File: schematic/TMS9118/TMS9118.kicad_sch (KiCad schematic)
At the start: 31 parts, among them CON1 PICERINO-EDGE, J1 Conn_Coaxial, J10 Conn_01x03, J2 Conn_01x02, J3 Conn_01x02, J8 Conn_01x08, J9 Conn_01x08, U1 TMS4416, U14 TMS9118NL, U3 TMS4416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

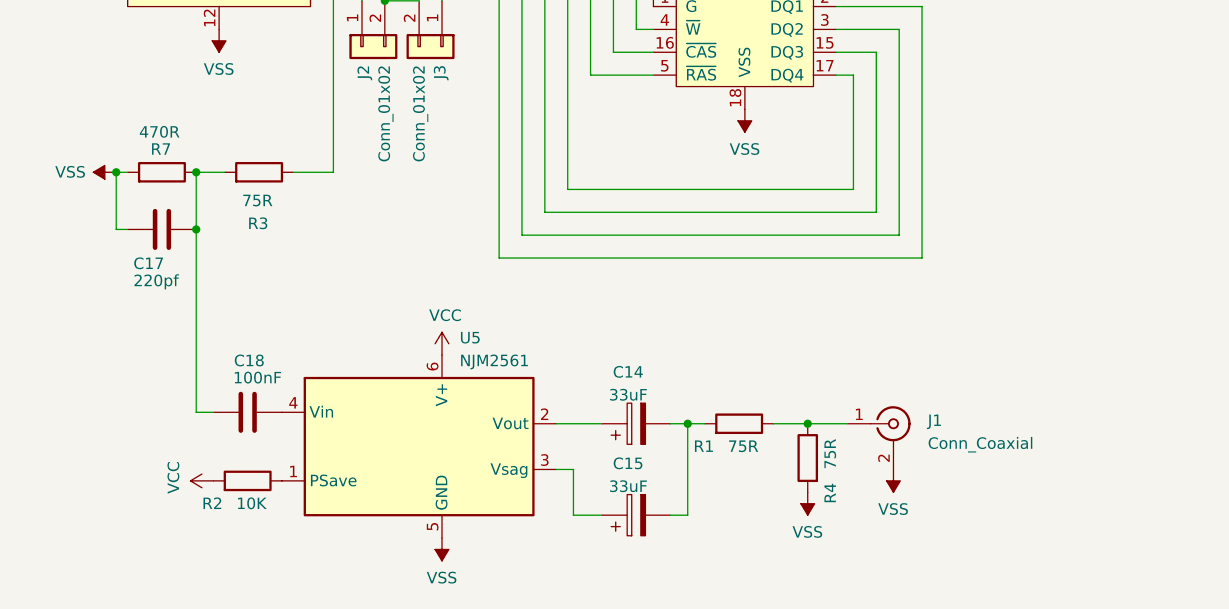
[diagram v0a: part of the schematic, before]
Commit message: added new switch and sample video chip to simplify video output. work in progress.
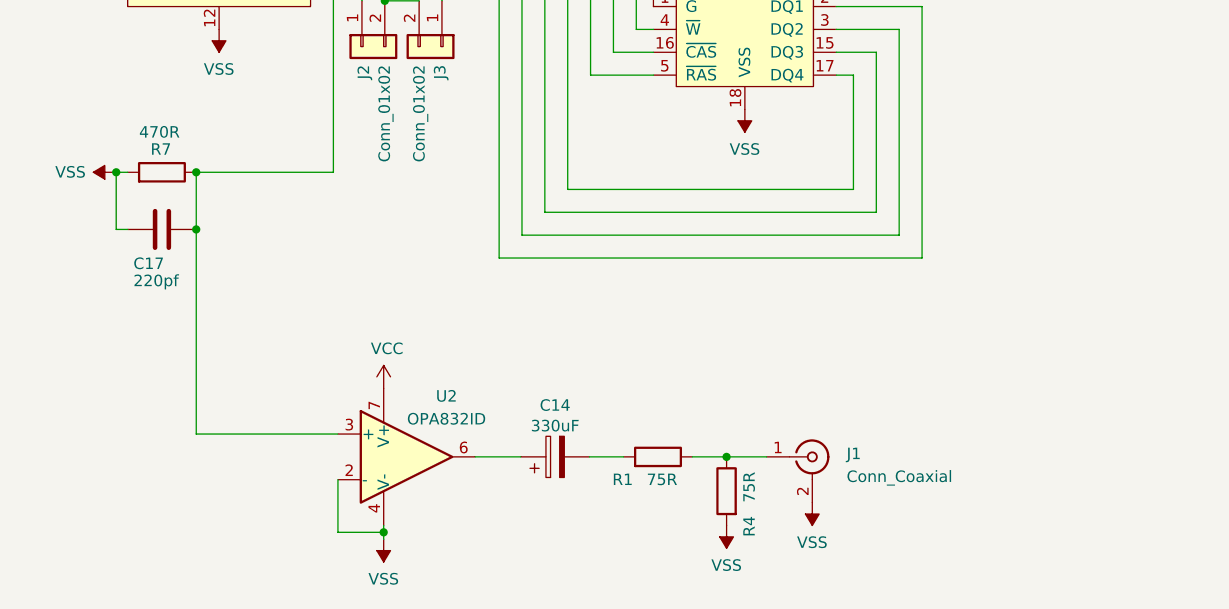
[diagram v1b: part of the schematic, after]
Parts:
- removed C15: 33uF, Capacitor_THT:CP_Radial_D5.0mm_P2.50mm, symbol Device:C_Polarized
- removed C18: 100nF, Capacitor_THT:C_Disc_D4.7mm_W2.5mm_P5.00mm, symbol Device:C
- removed R2: 10K, Resistor_THT:R_Axial_DIN0207_L6.3mm_D2.5mm_P7.62mm_Horizontal, symbol Device:R
- removed R3: 75R, Resistor_THT:R_Axial_DIN0207_L6.3mm_D2.5mm_P7.62mm_Horizontal, symbol Device:R
- removed U5: NJM2561, Package_TO_SOT_SMD:TSOT-23-6, symbol Video_II:NJM2561
- added U2: OPA832ID, Package_SO:SOIC-8_3.9x4.9mm_P1.27mm, symbol Amplifier_Operational:OPA842xD
- C14: value 33uF -> 330uF
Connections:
- net VCC: now also U2.7 (V+)
- net VSS: now also U2.2 (-), U2.4 (V-)
- net Y: now also C17.1, R7.1, U2.3 (+)
- net at C14.1: now also U2.6
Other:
- moved on the sheet: C14, J1, R1, R4

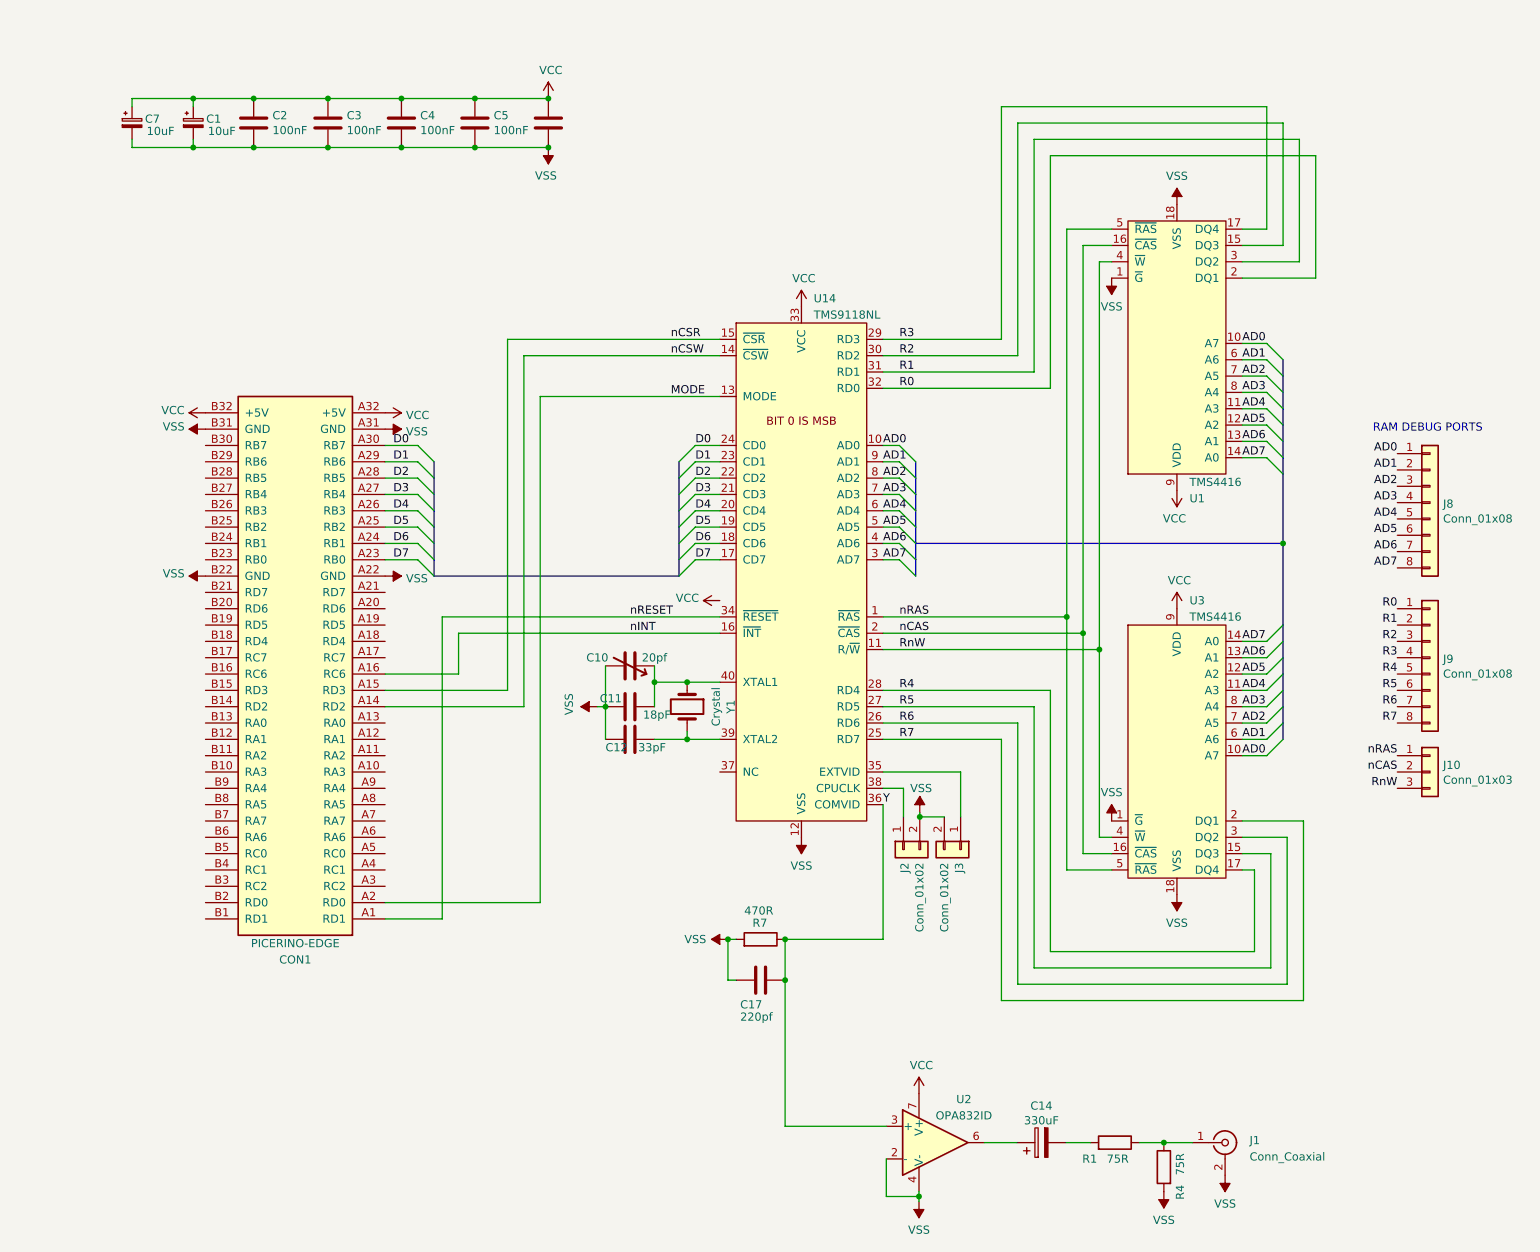
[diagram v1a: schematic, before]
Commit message: initial commit of v2 tms992X board
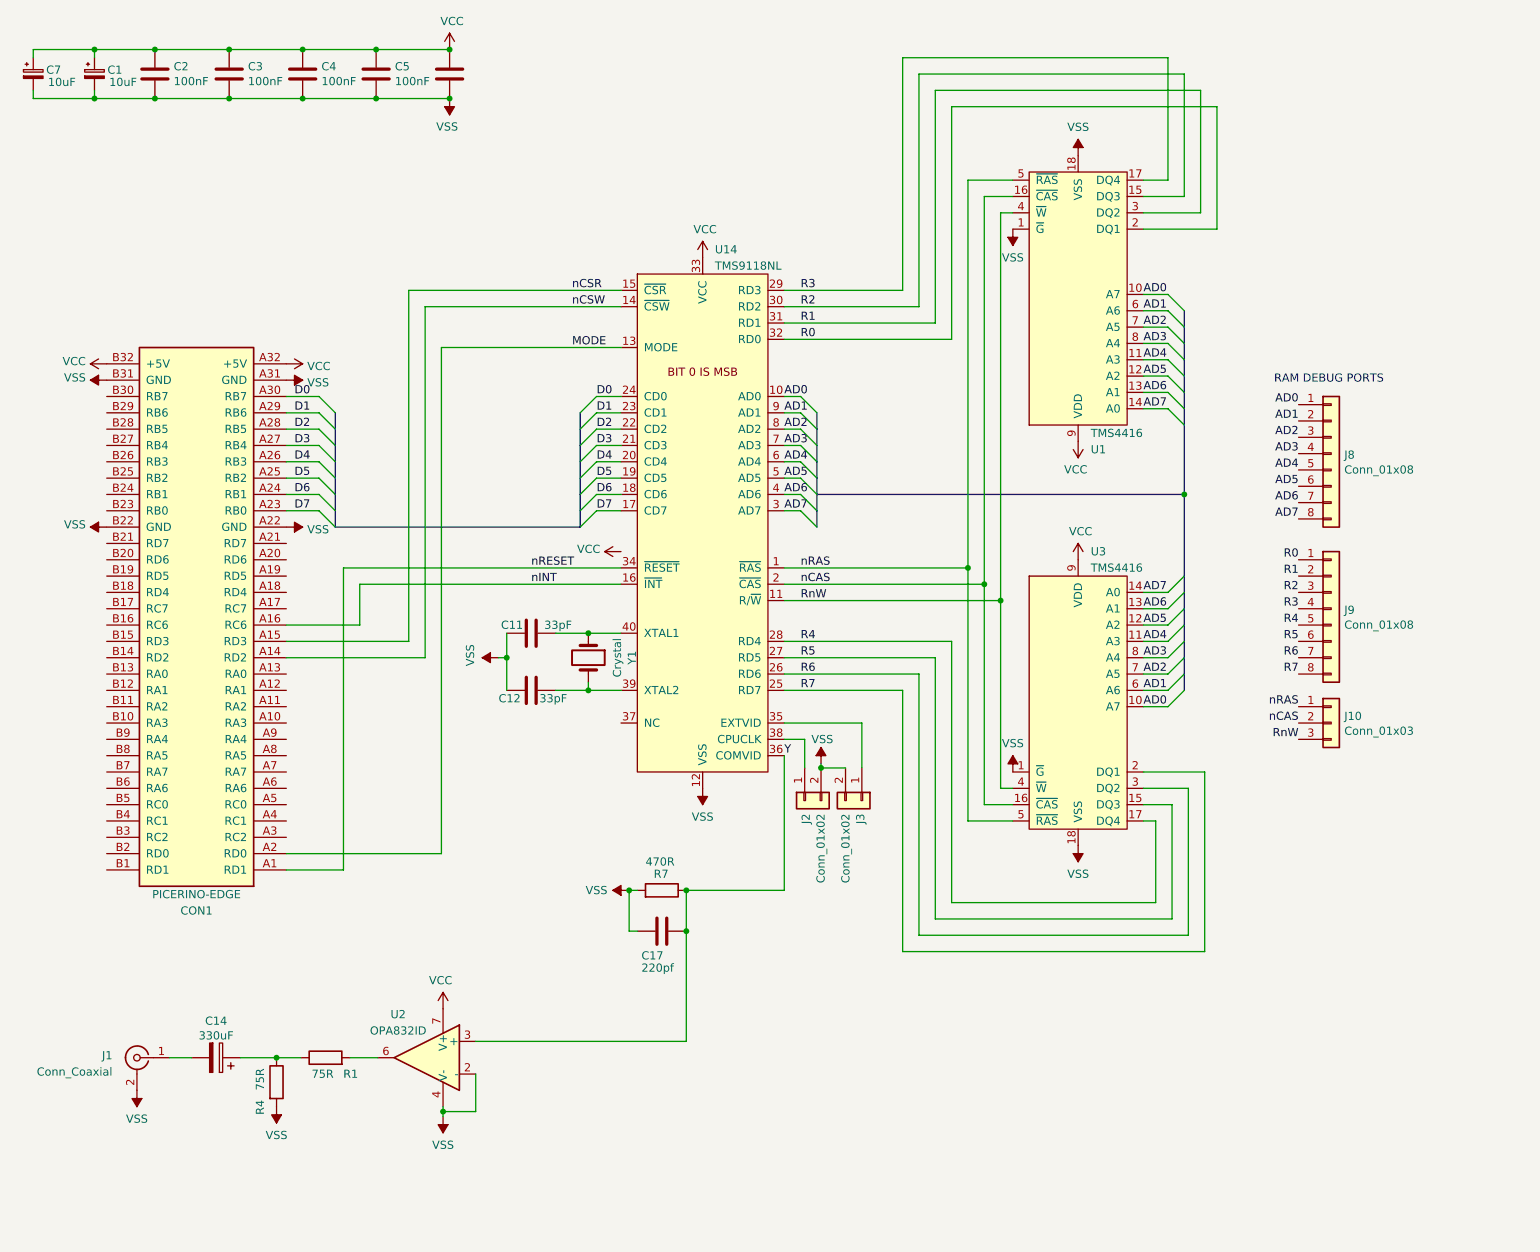
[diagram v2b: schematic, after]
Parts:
- removed C10: 20pf, Capacitor_THT:C_Rect_L10.0mm_W5.0mm_P5.00mm_P7.50mm, symbol Device:C_Variable
- C11: value 18pF -> 33pF
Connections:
- net at R1.1, R4.1: now also C14.1; no longer J1.1 (In)
- net at C14.2: now also J1.1 (In); no longer R1.2
- net at U2.6: now also R1.2; no longer C14.1
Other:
- moved on the sheet: C1, C11, C12, C14, C17, C2, C3, C4, C5, C7, CON1, J1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

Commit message: fixed tms9118 video output, opa832 failed
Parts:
- removed C14: 330uF, Capacitor_THT:CP_Radial_D5.0mm_P2.50mm, symbol Device:C_Polarized
- removed C17: 220pf, Capacitor_THT:C_Disc_D4.7mm_W2.5mm_P5.00mm, symbol Device:C
- removed U2: OPA832ID, Package_SO:SOIC-8_3.9x4.9mm_P1.27mm, symbol Amplifier_Operational:OPA842xD
- added Q1: 2N3904, Package_TO_SOT_THT:TO-92_Wide, symbol Transistor_BJT:2N3904
- R4: value 75R -> 100R
- R7: value 470R -> 510R
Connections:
- net VCC: now also Q1.3 (C)
- net VSS: now also R1.1; no longer R4.2
- net Y: now also R4.2; no longer R7.1
- net at J1.1 (In): now also R1.2, Q1.1 (E)
- net at R4.1: now also R7.1, Q1.2 (B); no longer R1.1
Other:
- moved on the sheet: J1, R1, R4
